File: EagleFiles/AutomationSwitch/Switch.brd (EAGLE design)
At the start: 90 x 40 mm, 28 parts, among them IC1 5V, U1 ATMEGA328P_PDIP

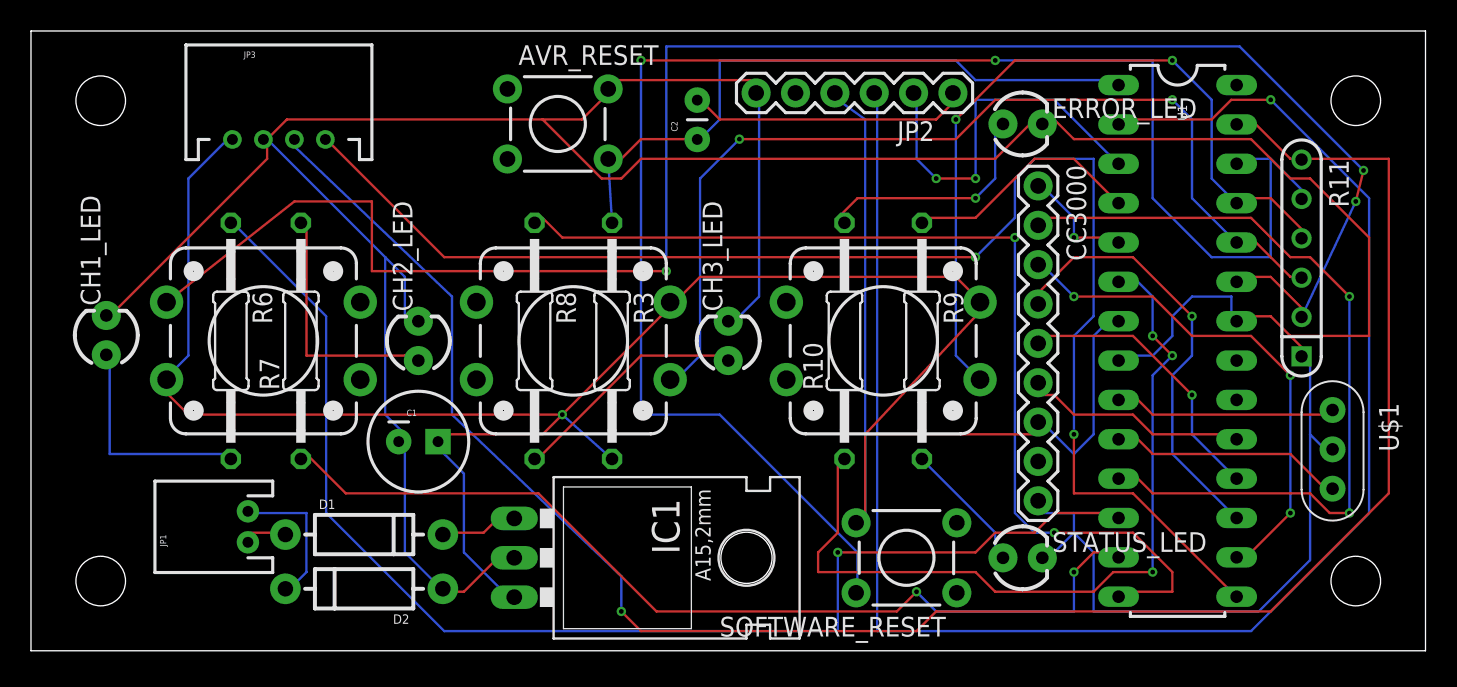
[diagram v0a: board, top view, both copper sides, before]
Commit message: Reworked routing and power
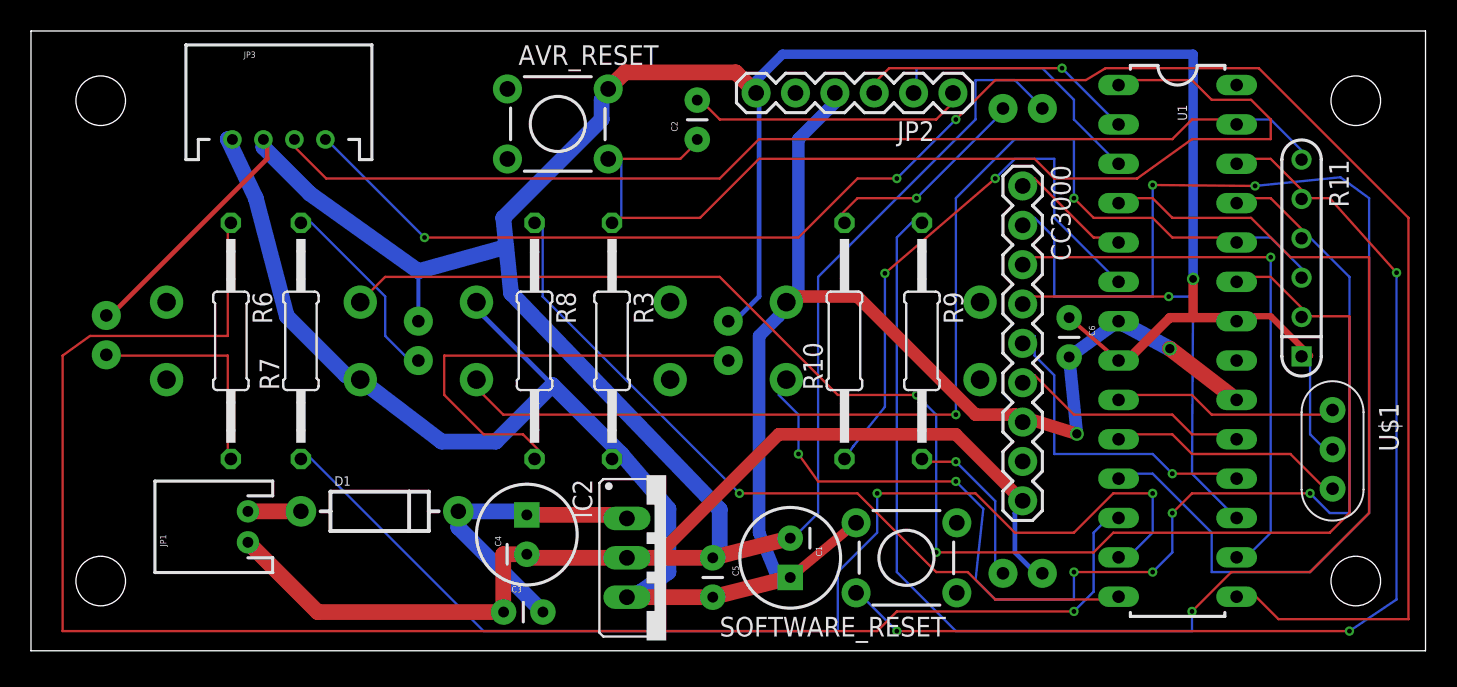
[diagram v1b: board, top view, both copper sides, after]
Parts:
- removed D2: (no value), SparkFun-DiscreteSemi:DIODE-1N4001
- removed IC1: 5V, SparkFun-PowerIC:78XXL
- added C3, C5, C6: 0.1uF, SparkFun-Passives:CAP-PTH-SMALL
- added C4: 10uF, SparkFun-Passives:CPOL-RADIAL-100UF-25V
- added IC2: 5V, v-reg:78XXS
- C2: value 100nf -> 0.1uF
- moved C1 25.1 mm to (49.0, 6.00), turned to 270 degrees
- moved D1 1.80 mm to (22.5, 9.00)
- moved CC3000 1.00 mm to (64.0, 30.0)
- moved ERROR_LED 1.00 mm to (64.0, 35.0), flipped to the bottom, turned to 180 degrees
- moved STATUS_LED 1.00 mm to (64.0, 5.00), flipped to the bottom, turned to 180 degrees
- flipped CH1_BTN to the bottom
- flipped CH1_LED to the bottom
- flipped CH2_BTN to the bottom
- flipped CH2_LED to the bottom
- flipped CH3_BTN to the bottom
- flipped CH3_LED to the bottom
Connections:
- removed net GND_IN: D2.C, JP1.2
- net 5V: now also C5.2, C6.2, IC2.OUT, U1.20; no longer IC1.OUT
- net GND: now also C3.1, C4.2, C5.1, C6.1, IC2.GND, JP1.1; no longer D2.A, IC1.GND
- net N$10: now also C3.2, C4.1, IC2.IN; no longer IC1.IN
- net VCC_IN: now also JP1.2; no longer JP1.1
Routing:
- net RX: track 109.4 -> 18.2 mm
- net STATUS_LED: track 16.3 -> 94.1 mm, vias 0 -> 1
- net CH4_IN: track 127.0 -> 70.9 mm, vias 1 -> 0
- net GND: track 246.3 -> 293.9 mm, vias 0 -> 1
- net SW_RESET: track 107.0 -> 71.8 mm, vias 2 -> 3
- net CH3_BTN: track 50.3 -> 79.9 mm, vias 2 -> 6
- net CH1_LED: track 82.6 -> 110.5 mm
- net RESET: track 42.9 -> 69.7 mm
- net CH4_OUT: track 92.2 -> 118.7 mm, vias 2 -> 3
- net VBEN: track 52.9 -> 76.7 mm
- net 5V: track 173.7 -> 151.8 mm, vias 1 -> 2
- net CH1_BTN: track 118.5 -> 99.8 mm, vias 3 -> 2
- net ERROR_LED: track 52.9 -> 36.3 mm, vias 3 -> 2
- net CH3_LED: track 65.9 -> 51.0 mm, vias 2 -> 1
- net N$10: track 5.28 -> 20.1 mm
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
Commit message: Optimized the Routing
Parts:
- added PULL_DOWN_CH4: SOLDERJUMPERNO, SparkFun-Passives:SJ_2S-NO
- JP3: value (none) -> CH4 Exp
- turned R6 to 90 degrees
- turned R8 to 90 degrees
- renumbered U$1 to OSC1
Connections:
- new net N$8: PULL_DOWN_CH4.2, R11.P$6
- net CH4_IN: now also PULL_DOWN_CH4.1; no longer R11.P$6
- net CH4_OUT: now also U1.28; no longer U1.15
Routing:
- net STATUS_LED: track 94.1 -> 17.7 mm, vias 1 -> 0
- net CH4_OUT: track 118.7 -> 61.2 mm, vias 3 -> 0
- net VBEN: track 76.7 -> 32.0 mm, vias 2 -> 1
- net CH3_BTN: track 79.9 -> 43.3 mm, vias 6 -> 0
- net GND: track 293.9 -> 263.8 mm
- net CH1_LED: track 110.5 -> 84.5 mm
- net RESET: track 69.7 -> 46.8 mm
- net MISO: track 21.5 -> 43.4 mm, vias 1 -> 0
- net N$3: track 29.5 -> 16.8 mm
- net CH2_LED: track 74.7 -> 62.2 mm, vias 2 -> 0
- net CH2_BTN: track 77.2 -> 67.7 mm
- net CH3_LED: track 51.0 -> 44.1 mm, vias 1 -> 0
- net SW_RESET: track 71.8 -> 68.3 mm, vias 3 -> 0
- net ERROR_LED: track 36.3 -> 39.6 mm, vias 2 -> 1
- net N$8: track 0.00 -> 2.73 mm
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
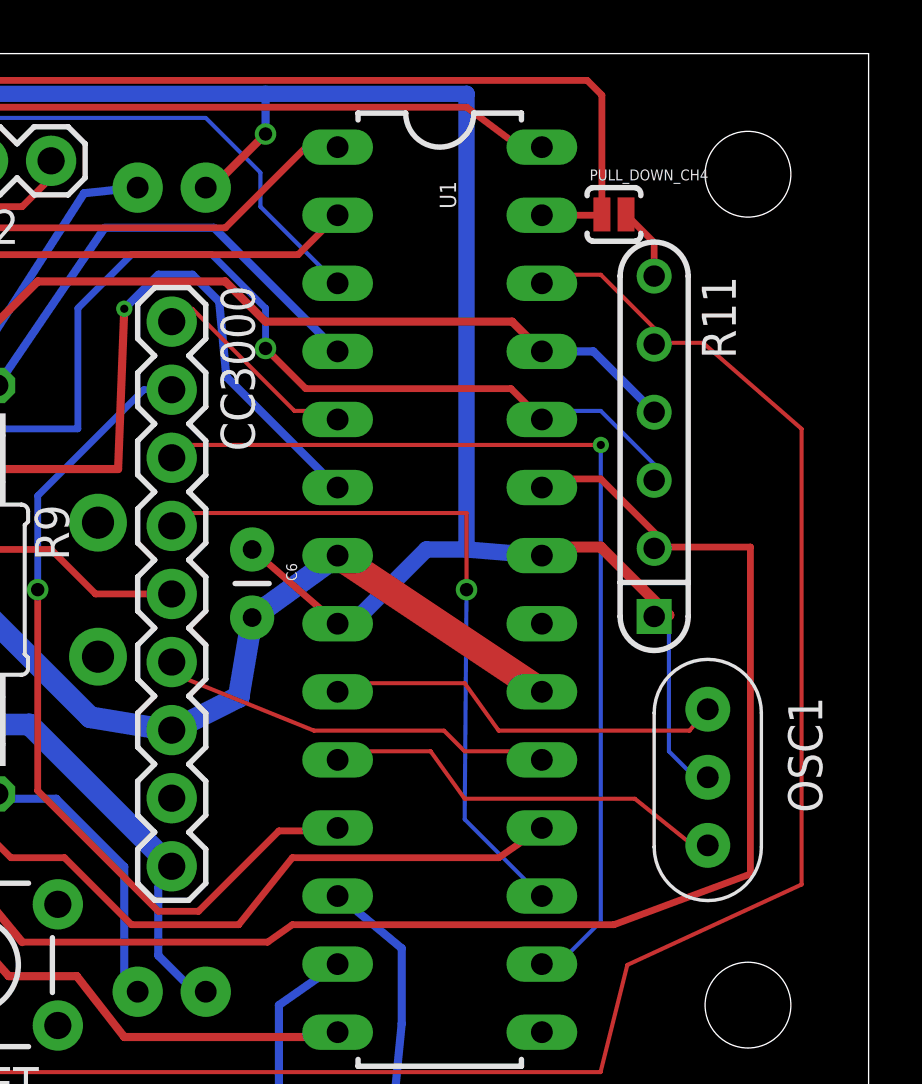
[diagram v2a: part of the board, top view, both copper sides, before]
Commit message: Optimize Routing
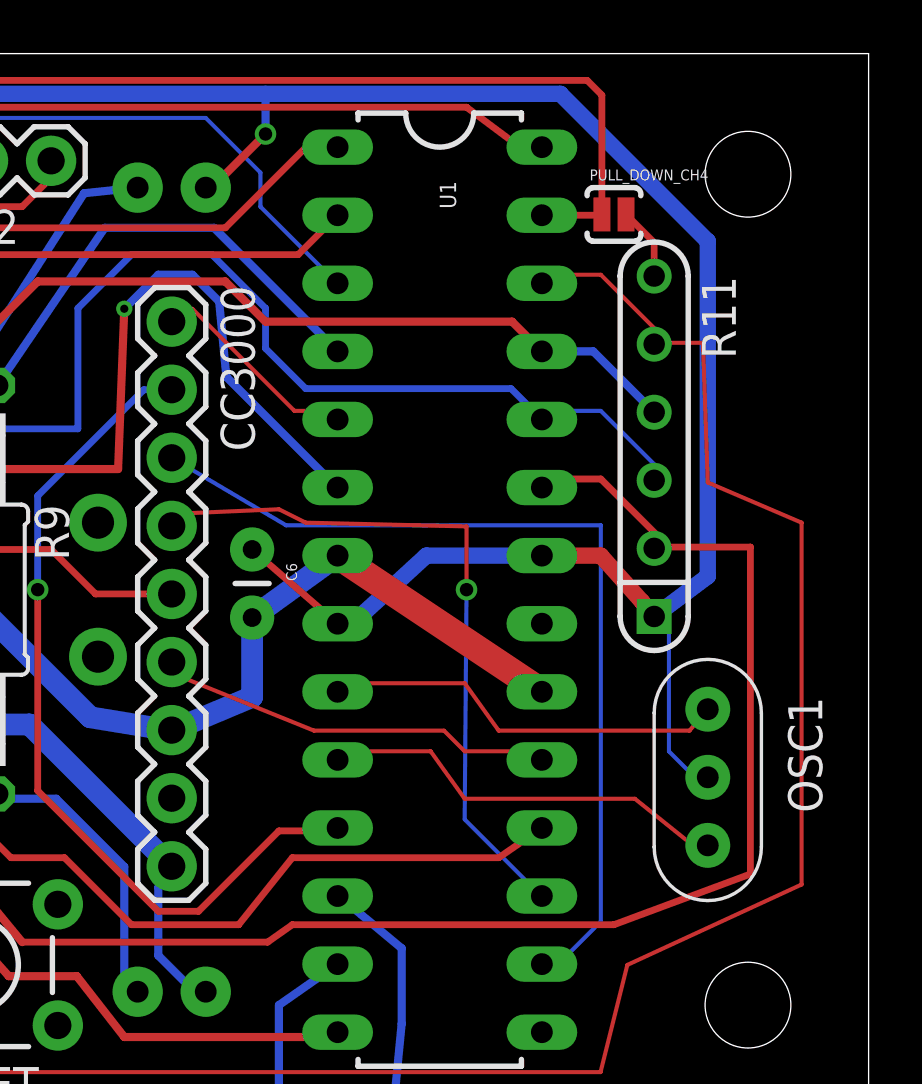
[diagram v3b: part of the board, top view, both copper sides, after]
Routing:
- net GND: track 263.8 -> 271.8 mm
- net CS: track 36.7 -> 34.3 mm, vias 1 -> 0
- net SW_RESET: track 68.3 -> 68.9 mm
- net CH2_BTN: vias 2 -> 1

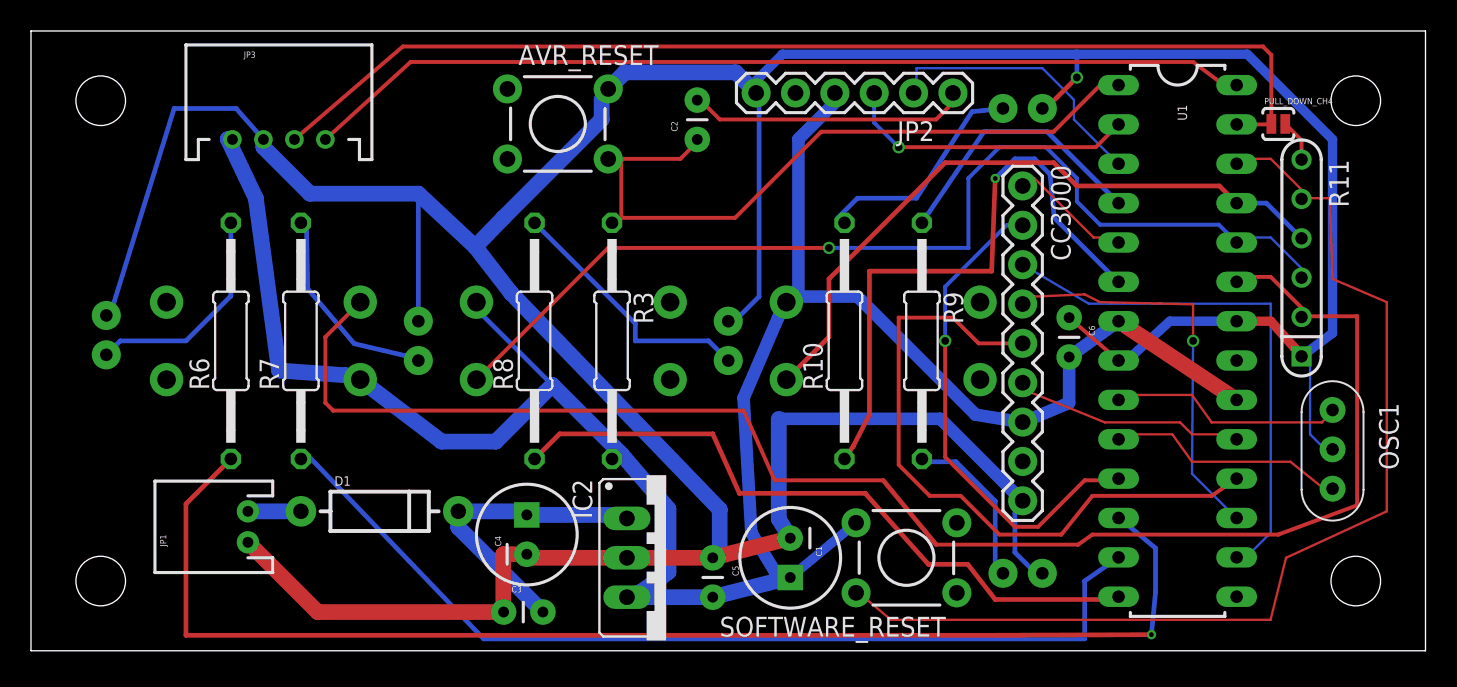
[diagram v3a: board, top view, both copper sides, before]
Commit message: Rework Traces
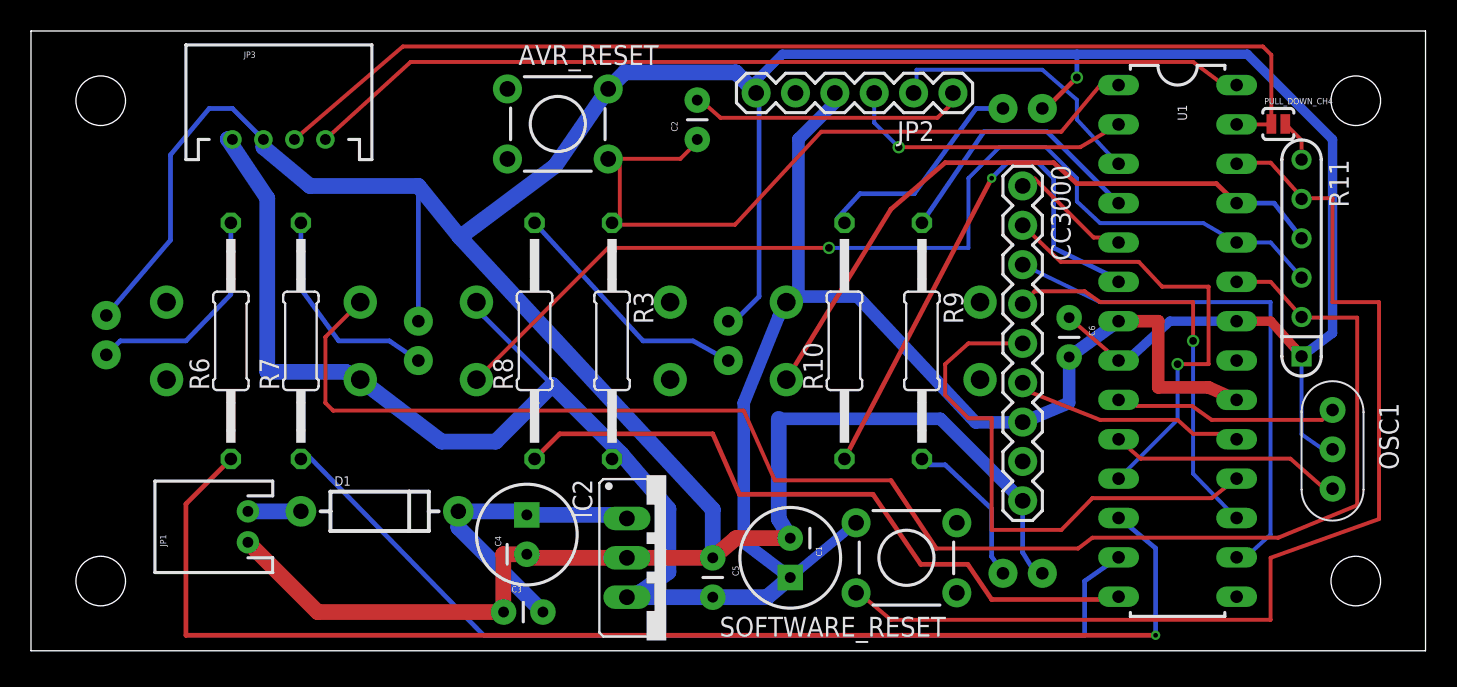
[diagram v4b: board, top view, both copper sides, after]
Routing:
- net MISO: track 43.4 -> 35.4 mm
- net 5V: track 150.3 -> 155.3 mm
- net ERROR_LED: track 39.6 -> 34.5 mm
- net VBEN: track 32.0 -> 29.6 mm
- net CH2_BTN: track 67.7 -> 66.3 mm
- net GND: track 271.8 -> 270.7 mm
- net SW_RESET: track 68.9 -> 69.9 mm
- net RESET: track 46.8 -> 47.6 mm
- net N$2: track 11.0 -> 10.1 mm
- net N$6: track 15.1 -> 14.4 mm
- net N$3: track 16.8 -> 16.2 mm
- net CH3_BTN: track 43.3 -> 42.6 mm
- net N$4: track 13.4 -> 13.9 mm

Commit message: Label Rework
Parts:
- moved PULL_DOWN_CH4 1.58 mm to (81.0, 35.5)
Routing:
- net GND: track 270.7 -> 266.3 mm
- net 5V: track 155.3 -> 151.6 mm
- net SW_RESET: track 69.9 -> 66.7 mm
- net CH2_LED: track 61.8 -> 60.1 mm
- net CH1_BTN: track 101.2 -> 99.9 mm
- net MISO: track 35.4 -> 34.3 mm
- net N$8: track 2.73 -> 3.86 mm
- net CH2_BTN: track 66.3 -> 65.3 mm
- net CH1_LED: track 84.8 -> 83.8 mm
- net MOSI: track 26.7 -> 26.1 mm
- net VBEN: track 29.6 -> 29.0 mm
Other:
- board text added: "Wifi Switch Rev 1"

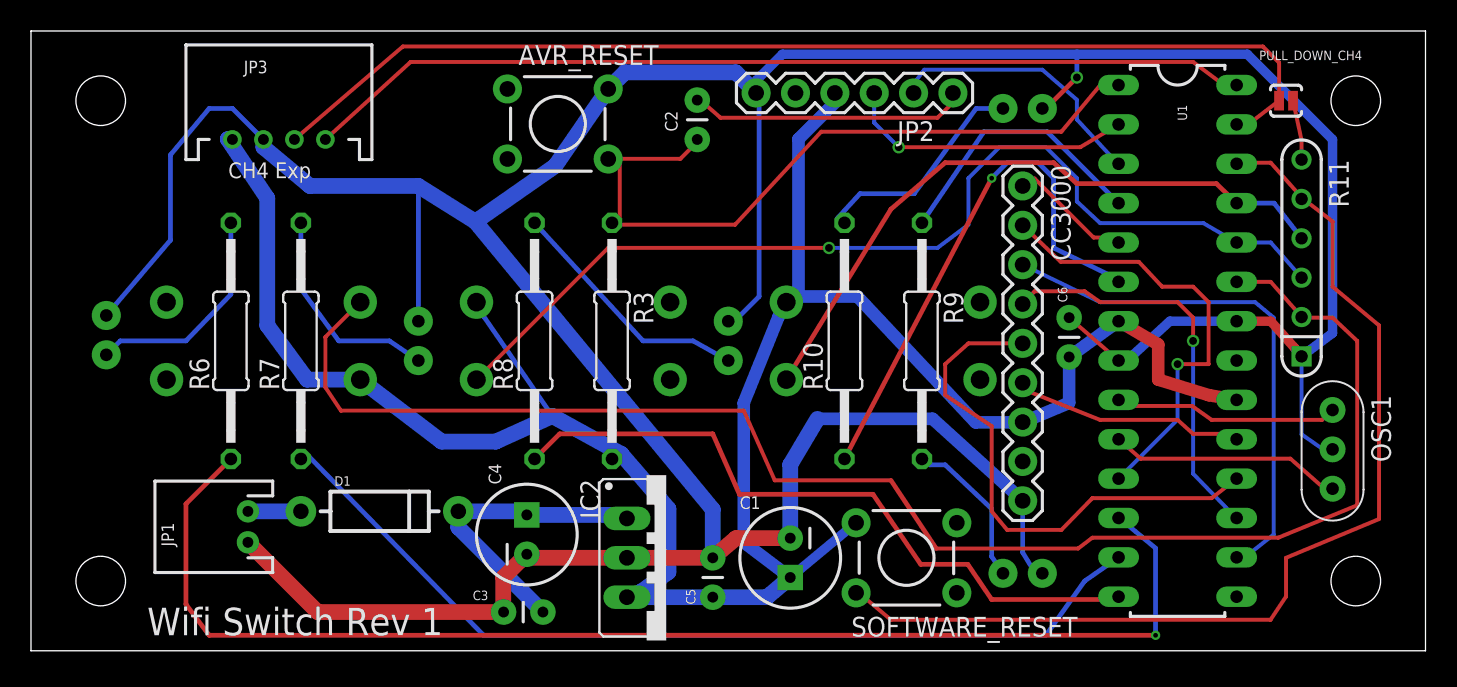
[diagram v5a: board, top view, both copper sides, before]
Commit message: Moved Regulator to fix clearance issues with CC3K Module
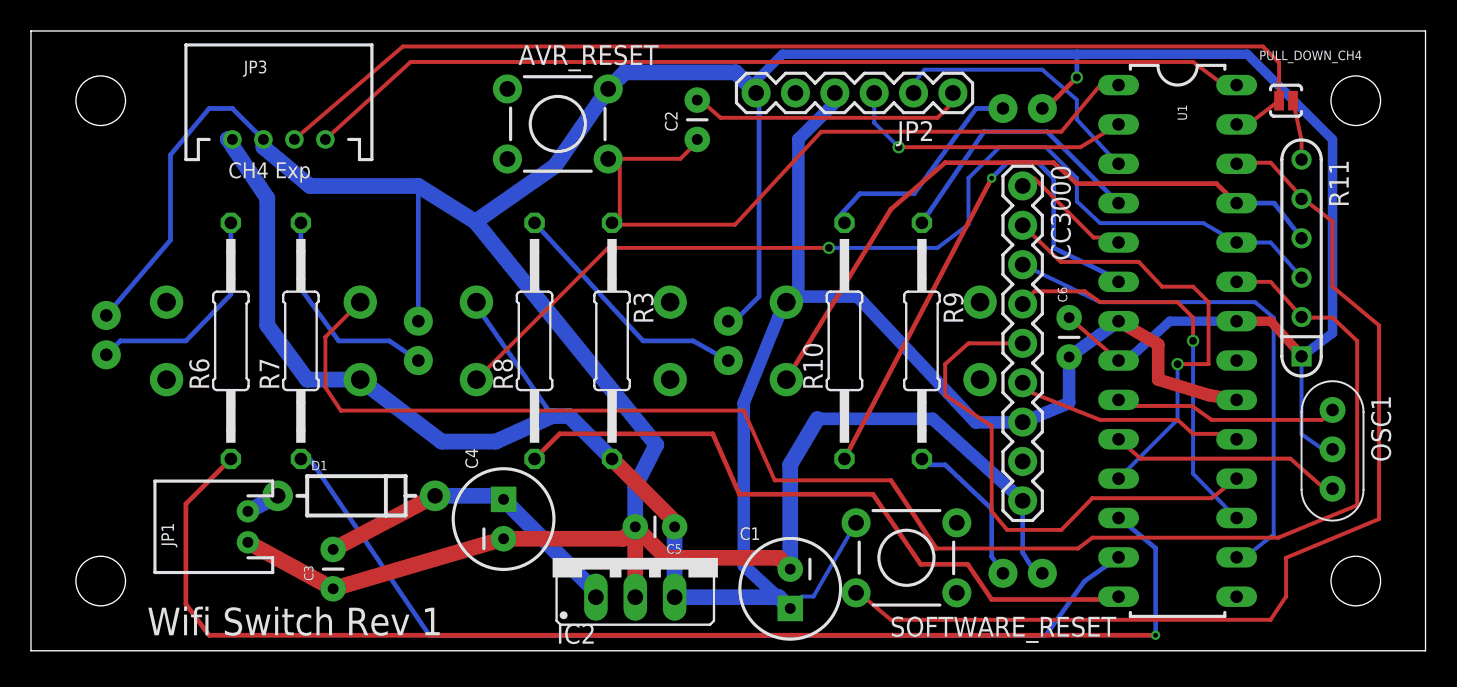
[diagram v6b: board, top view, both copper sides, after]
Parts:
- moved C3 11.1 mm to (19.5, 4.00), turned to 90 degrees
- moved C5 5.39 mm to (39.0, 8.00), turned to 0 degrees
- moved C1 2.00 mm to (49.0, 4.00)
- moved IC2 2.00 mm to (39.0, 6.00), turned to 0 degrees
- moved C4 1.80 mm to (30.5, 8.50)
- moved D1 1.80 mm to (21.0, 10.0)
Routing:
- net 5V: track 151.6 -> 149.9 mm
- net CH2_LED: track 60.1 -> 61.4 mm
- net VCC_IN: track 3.42 -> 2.16 mm
- net N$10: track 20.1 -> 20.7 mm

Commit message: Final Cleanup
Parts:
- C4: device SparkFun-Passives:CPOL-RADIAL-100UF-25V -> SparkFun-Passives:CPOL-RADIAL-10UF-25V
- CH1_LED, CH2_LED, CH3_LED: value (none) -> Blue
- ERROR_LED: value (none) -> Red
- R10, R6, R7, R8, R9: value (none) -> 2k
- STATUS_LED: value (none) -> Green
- moved JP1 4.61 mm to (10.5, 11.0)
- moved JP3 2.00 mm to (16.0, 36.0)
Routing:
- net VCC_IN: track 2.16 -> 10.1 mm
- net CH1_LED: track 83.8 -> 79.7 mm
- net GND: track 266.7 -> 270.5 mm
- net 5V: track 149.9 -> 147.5 mm
- net CH4_IN: track 71.9 -> 73.3 mm
- net CH4_OUT: track 61.2 -> 62.5 mm
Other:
- board text added: "Wifi Switch Rev1"
- board text removed: "Wifi Switch Rev 1"
